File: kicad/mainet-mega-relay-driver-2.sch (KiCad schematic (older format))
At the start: 8 parts, among them J31 Screw_Terminal_01x03, K2 SANYOU_SRD_Form_C, Q2 2N3904, U3 4N37

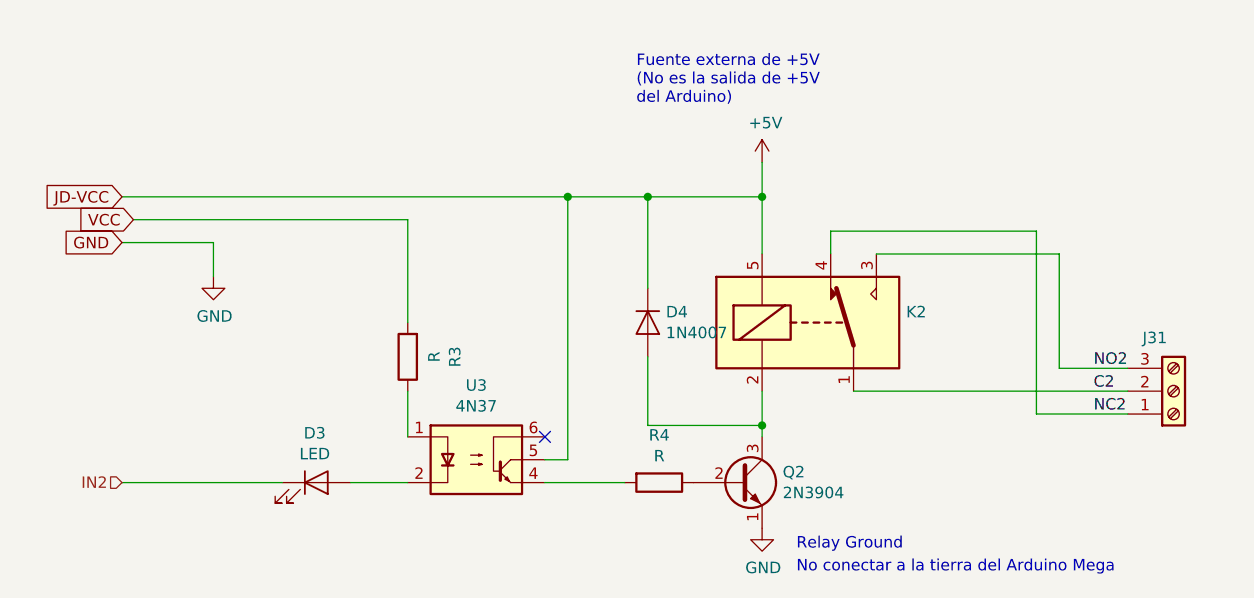
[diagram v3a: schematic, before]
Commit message: KICAD: Actualización de esquematicos del módulo de 8 relés de control
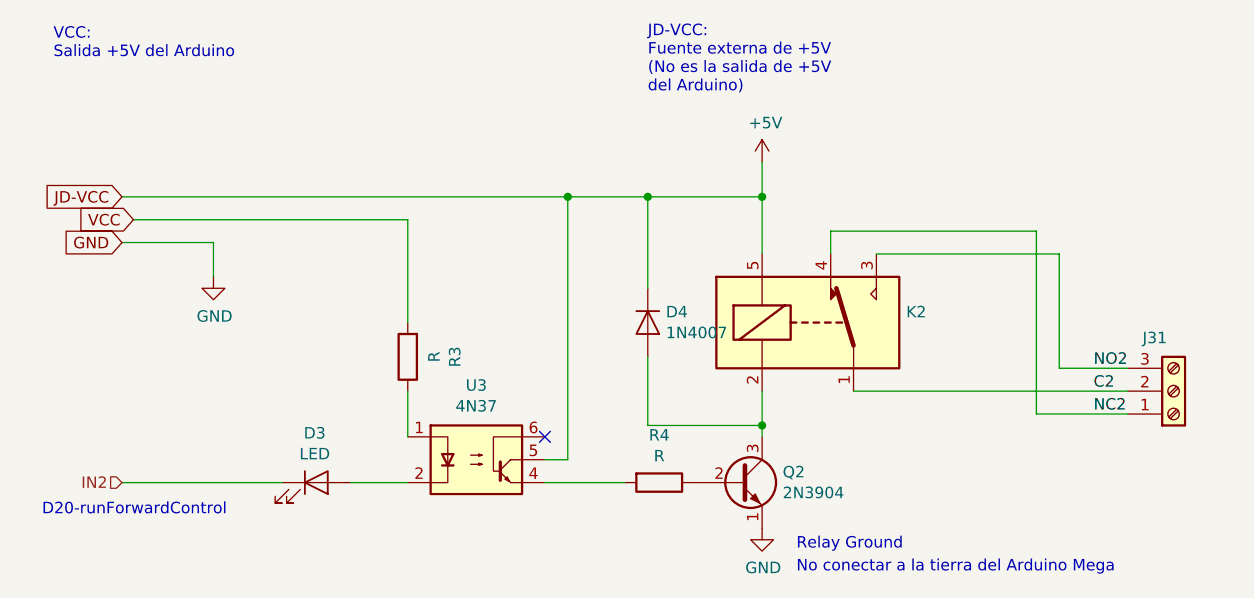
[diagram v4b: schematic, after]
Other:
- note added: "D20-runForwardControl"
- note added: "JD-VCC:\nFuente externa de +5V\n(No es la salida de +5V \ndel Arduino)"
- note added: "VCC:\nSalida +5V del Arduino"
- note removed: "Fuente externa de +5V\n(No es la salida de +5V \ndel Arduino)"
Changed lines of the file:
@@
 EESchema Schematic File Version 4
 LIBS:mainet-mega-cache
-LIBS:mainet-mega-5V-to-mp-10v-cache
 EELAYER 30 0
 EELAYER END
 $Descr A4 11693 8268
 encoding utf-8
-Sheet 9 21
-Title ""
-Date ""
+Sheet 8 21
+Title "Relay driver 2"
+Date "2021-02-02"
 Rev ""
 Comp ""
@@
 	1    0    0    -1
 $EndComp
-Text Notes 5750 2500 0    50   ~ 0
-Fuente externa de +5V\n(No es la salida de +5V \ndel Arduino)
 Text Notes 6450 4450 0    50   ~ 0
 Relay Ground\n
@@
 Text GLabel 3500 3100 0    50   Input ~ 0
 GND
+Text Notes 3150 4300 0    50   ~ 0
+D20-runForwardControl
+Text Notes 5800 2450 0    50   ~ 0
+JD-VCC:\nFuente externa de +5V\n(No es la salida de +5V \ndel Arduino)
+Text Notes 3200 2300 0    50   ~ 0
+VCC:\nSalida +5V del Arduino
 $EndSCHEMATC
